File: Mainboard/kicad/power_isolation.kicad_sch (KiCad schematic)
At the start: 59 parts, among them J4 1935161, U11 MC78M15CDTRKG, U12 MC79M15CDTRKG, U13 MC79M15CDTRKG, U14 MC78M15CDTRKG, U15 MCP1826T-5002E/ET, U16 MCP1826T-3302E/ET

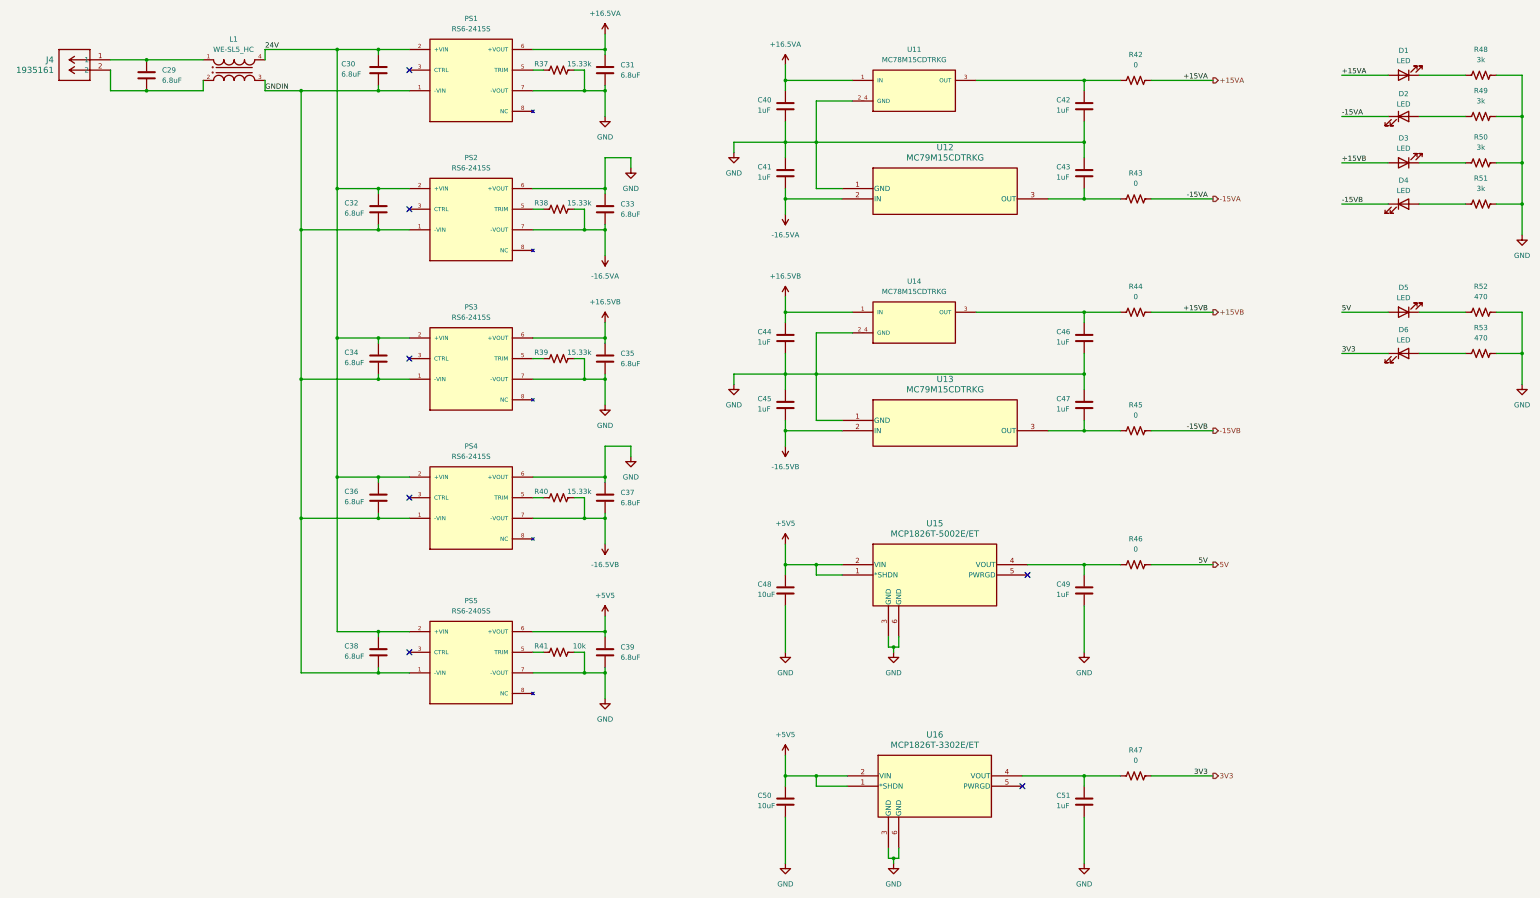
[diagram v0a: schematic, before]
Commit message: Correct LED direction and processor pins
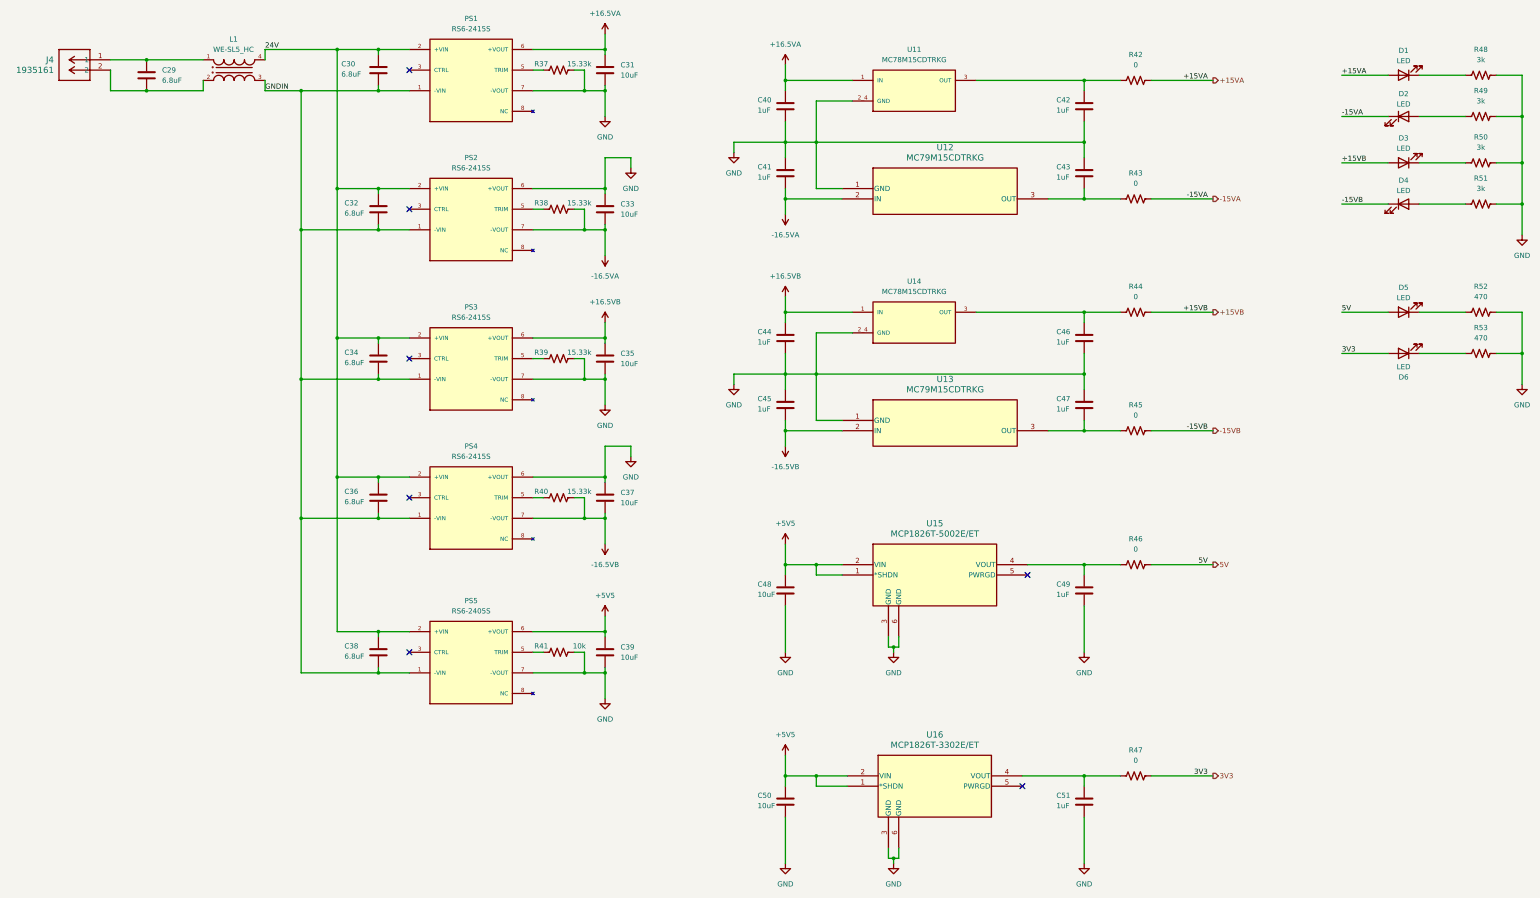
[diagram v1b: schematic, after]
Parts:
- C31, C33, C35, C37, C39: value 6.8uF -> 10uF
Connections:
- net 3V3: now also D6.2 (A); no longer D6.1 (K)
- net at R53.1: now also D6.1 (K); no longer D6.2 (A)
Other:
- moved on the sheet: D6
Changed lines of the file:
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@@
 	(wire
 		(pts
+			(xy 345.44 99.06) (xy 356.87 99.06)
+		)
+		(stroke
+			(width 0)
+			(type default)
+		)
+	)
+	(wire
+		(pts
 			(xy 107.95 95.25) (xy 107.95 96.52)
 		)
@@
 	(wire
 		(pts
-			(xy 345.44 99.06) (xy 356.87 99.06)
-		)
-		(stroke
-			(width 0)
-			(type default)
-		)
-	)
-	(wire
-		(pts
 			(xy 163.83 121.92) (xy 163.83 129.54)
 		)
@@
 			)
 		)
-		(property "Value" "6.8uF"
+		(property "Value" "10uF"
 			(at 167.64 64.7699 0)
 			(effects
@@
 	(symbol
 		(lib_id "Device:LED")
-		(at 360.68 99.06 0)
+		(at 360.68 99.06 180)
 		(unit 1)
 		(exclude_from_sim no)
@@
 		(dnp no)
 		(property "Reference" "D6"
-			(at 360.68 93.218 0)
+			(at 360.68 104.902 0)
 			(effects
 				(font
@@
 		)
 		(property "Value" "LED"
-			(at 360.68 95.758 0)
+			(at 360.68 102.362 0)
 			(effects
 				(font
@@
 			)
 		)
-		(property "Value" "6.8uF"
+		(property "Value" "10uF"
 			(at 167.64 101.5999 0)
 			(effects
@@
 			)
 		)
-		(property "Value" "6.8uF"
+		(property "Value" "10uF"
 			(at 167.64 30.4799 0)
 			(effects
@@
 			)
 		)
-		(property "Value" "6.8uF"
+		(property "Value" "10uF"
 			(at 167.64 135.8899 0)
 			(effects
@@
 			)
 		)
-		(property "Value" "6.8uF"
+		(property "Value" "10uF"
 			(at 167.64 173.9899 0)
 			(effects
